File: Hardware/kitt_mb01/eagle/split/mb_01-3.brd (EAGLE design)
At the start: 160 x 100 mm, 15 parts, among them IC3.01 LSM9DS1

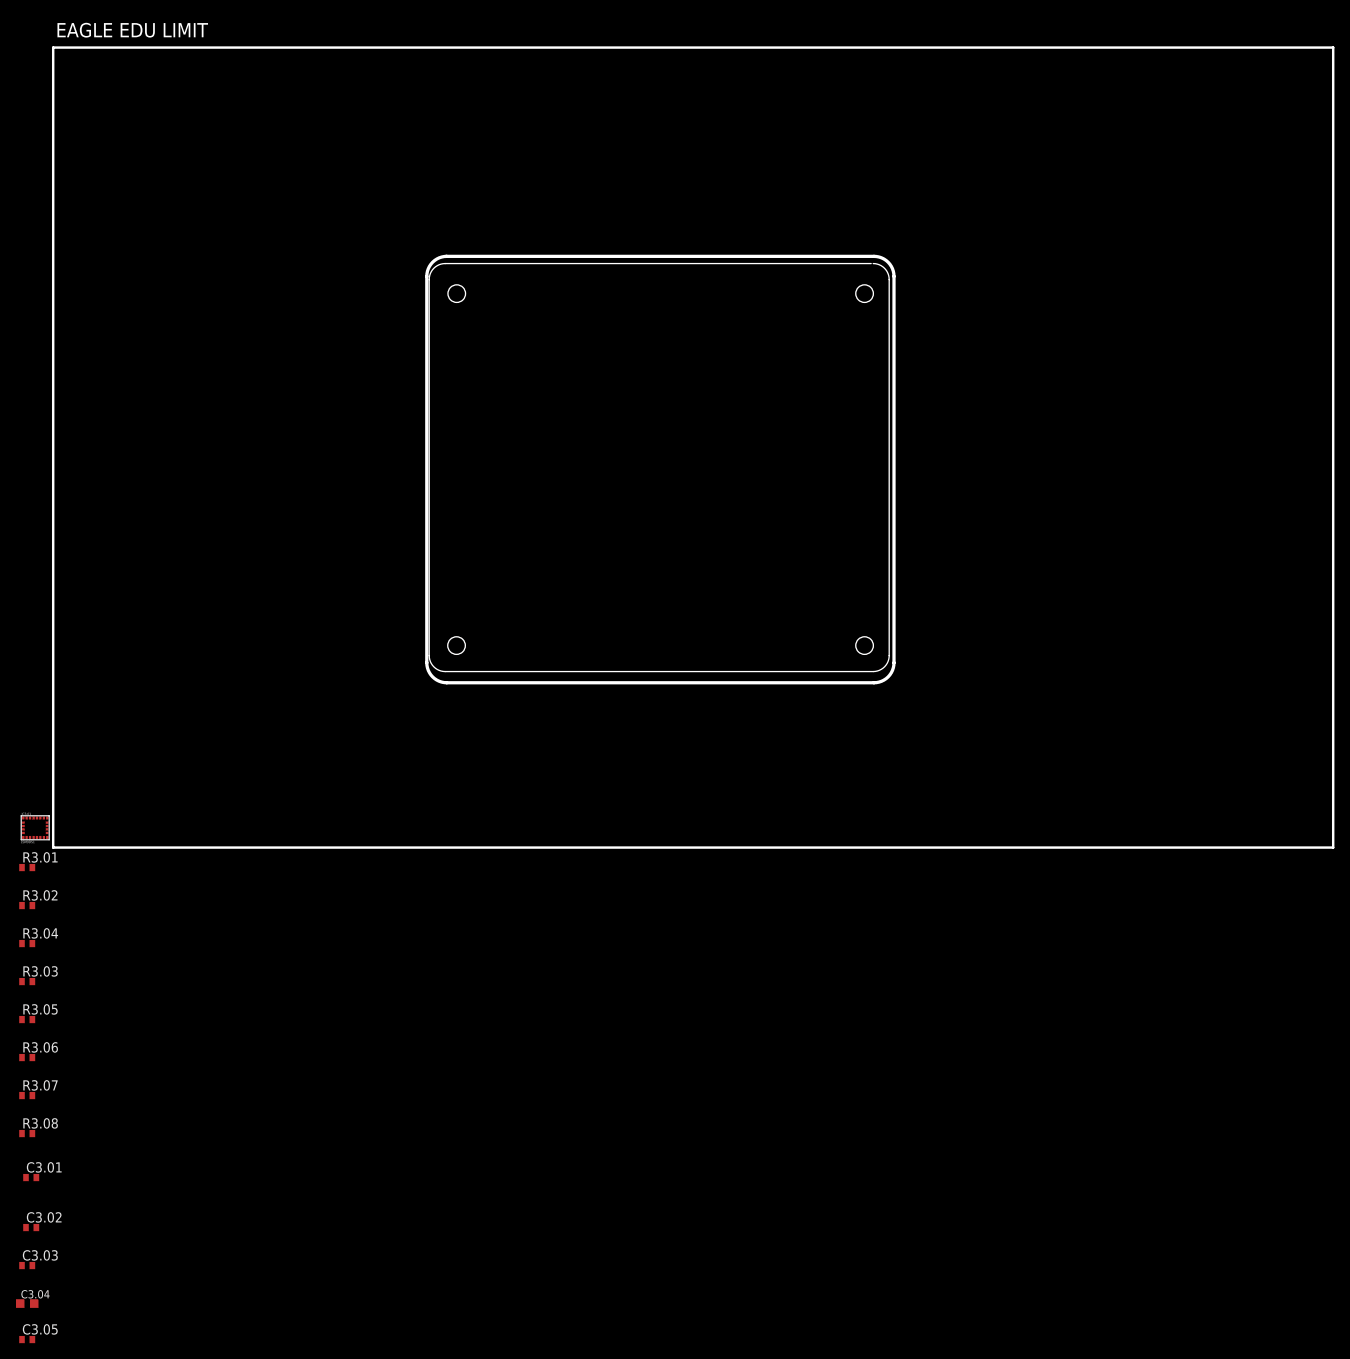
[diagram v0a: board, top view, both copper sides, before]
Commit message: did route+place for subsection 1 and 3
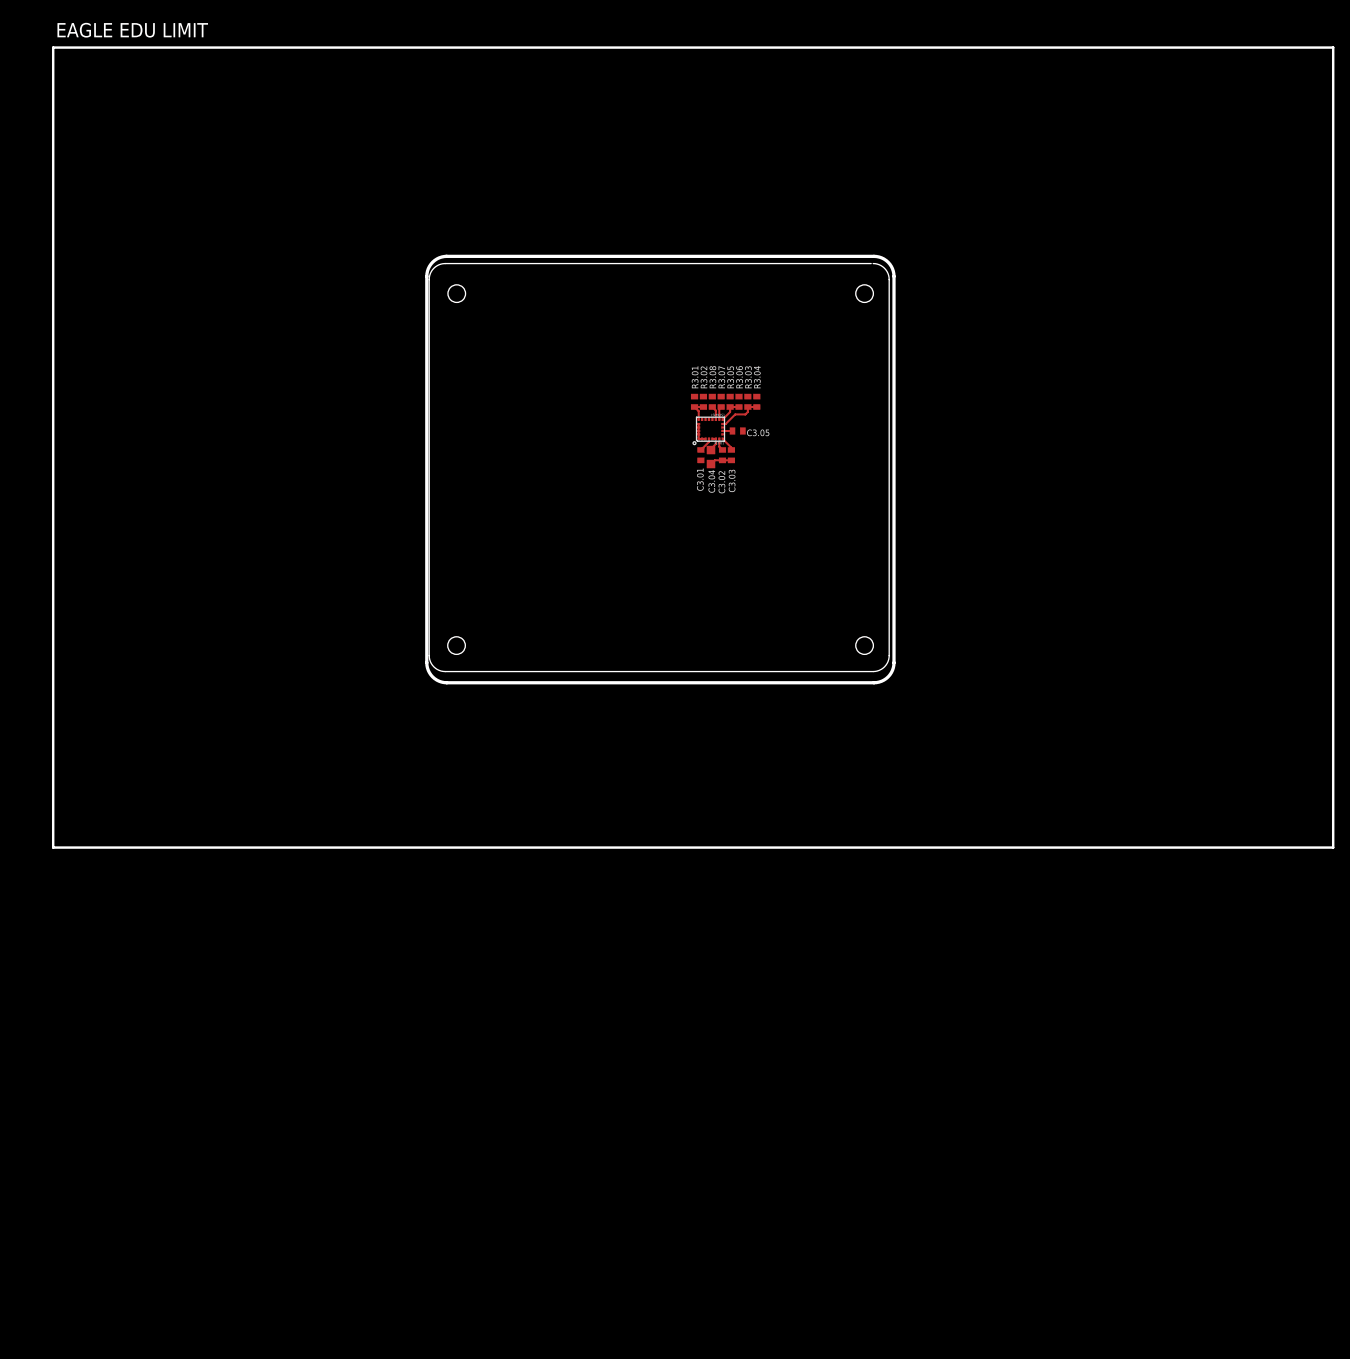
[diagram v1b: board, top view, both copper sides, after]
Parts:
- C3.03, C3.05: value 10nF -> 100nF
- C3.04: device rcl:C0603K -> resistor:C0603K
- moved C3.05 144.2 mm to (85.6, 52.1)
- moved C3.04 136.0 mm to (82.2, 48.8), turned to 270 degrees
- moved C3.03 134.2 mm to (84.8, 49.1), turned to 270 degrees
- moved C3.02 129.6 mm to (83.7, 49.1), turned to 270 degrees
- moved R3.08 125.3 mm to (82.4, 55.7), turned to 90 degrees
- moved C3.01 123.1 mm to (81.0, 49.1), turned to 270 degrees
- moved R3.07 122.7 mm to (83.5, 55.7), turned to 90 degrees
- moved R3.06 121.0 mm to (85.7, 55.7), turned to 270 degrees
- moved R3.05 117.0 mm to (84.6, 55.7), turned to 90 degrees
- moved R3.03 115.6 mm to (86.8, 55.7), turned to 90 degrees
- moved R3.04 113.6 mm to (87.9, 55.7), turned to 270 degrees
- moved R3.02 105.4 mm to (81.3, 55.7), turned to 270 degrees
- moved IC3.01 101.9 mm to (83.7, 53.5), turned to 180 degrees
- moved R3.01 101.7 mm to (80.2, 55.7), turned to 90 degrees
- moved U$1 43.1 mm to (51.1, 25.7)
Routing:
- net N$23: track 0.00 -> 5.50 mm
- net GND: track 0.00 -> 5.47 mm
- net +3V3: track 0.00 -> 5.10 mm
- net N$26: track 0.00 -> 3.04 mm
- net N$17: track 0.00 -> 2.88 mm
- net N$1: track 0.00 -> 1.79 mm
- net N$27: track 0.00 -> 1.74 mm
- net N$24: track 0.00 -> 1.65 mm
- net N$6: track 0.00 -> 1.53 mm
